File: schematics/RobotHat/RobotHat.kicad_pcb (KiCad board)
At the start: 2 copper layers, 65 x 63.5 mm, 43 parts, among them J1 9Vin, J10 MotorA, J11 MotorB, J12 Raspberry_Pi_2_3, J2 5Vout, J3 3V3out, J4 ATMega_ICSP, J5 ATMega_FTDI, J6 I2C, J7 ATMega AnalogPins, J8 WheelEncA, J9 WheelEncB, SW1 Reset, U1 ATmega328P-MU, U2 LM2596S-5, U3 TB6612FNG, Y1 16MHz

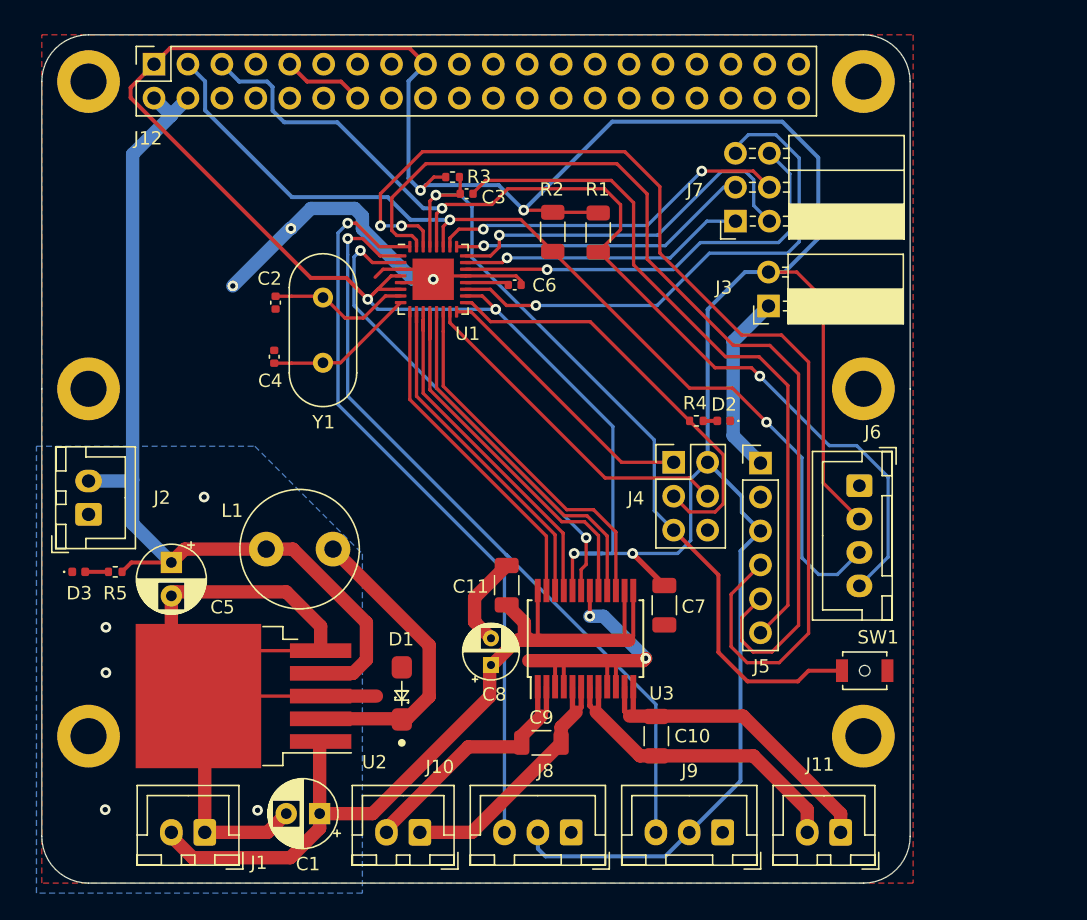
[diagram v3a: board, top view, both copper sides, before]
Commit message: Arduino runs at 5v with logic level shifter on i2c bus
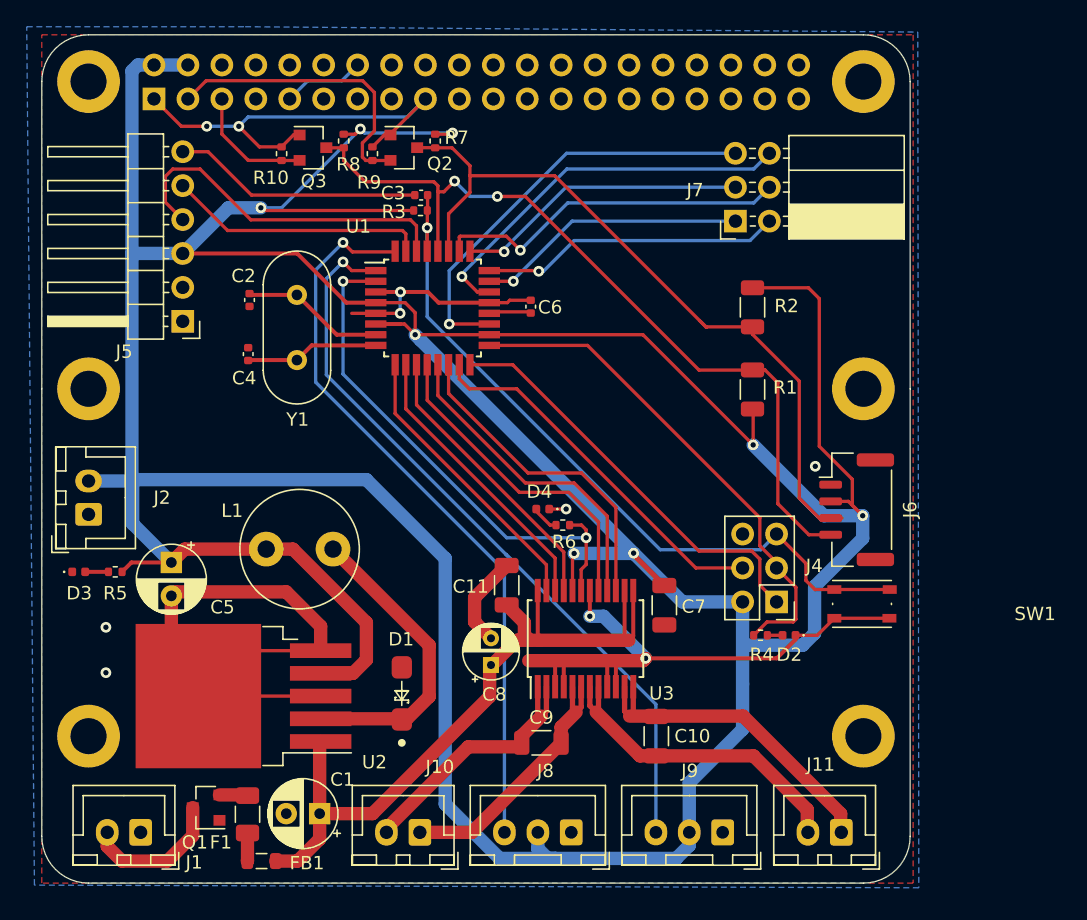
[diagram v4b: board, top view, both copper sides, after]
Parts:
- removed J3: 3V3out, Connector_PinSocket_2.54mm:PinSocket_1x02_P2.54mm_Horizontal
- added D4: GREEN, Diode_SMD:D_0402_1005Metric, F.Cu at (87.8, 77.5)
- added F1: Polyfuse, Fuse:Fuse_1206_3216Metric, F.Cu at (65.7, 100.3)
- added FB1: Ferrite_Bead, Inductor_SMD:L_0805_2012Metric, F.Cu at (66.8, 103.8)
- added Q1: AO3401A, Package_TO_SOT_SMD:SOT-23, F.Cu at (62.6, 99.8)
- added Q2: 2N7002, Package_TO_SOT_SMD:SOT-23, F.Cu at (77.4, 50.5)
- added Q3: 2N7002, Package_TO_SOT_SMD:SOT-23, F.Cu at (70.6, 50.5)
- added R10: 4.7k, Resistor_SMD:R_0402_1005Metric, F.Cu at (68.2, 50.9)
- added R6: 330, Resistor_SMD:R_0402_1005Metric, F.Cu at (89.3, 78.7)
- added R7: 4.7k, Resistor_SMD:R_0402_1005Metric, F.Cu at (79.8, 50.0)
- added R8: 4.7k, Resistor_SMD:R_0402_1005Metric, F.Cu at (72.9, 50.0)
- added R9: 4.7k, Resistor_SMD:R_0402_1005Metric, F.Cu at (75.0, 50.9)
- J12: moved to B.Cu
- J5: footprint Connector_PinHeader_2.54mm:PinHeader_1x06_P2.54mm_Vertical -> Connector_PinHeader_2.54mm:PinHeader_1x06_P2.54mm_Horizontal
- J6: footprint Connector_JST:JST_XH_B4B-XH-A_1x04_P2.50mm_Vertical -> Connector_JST:JST_GH_BM04B-GHS-TBT_1x04-1MP_P1.25mm_Vertical
- SW1: footprint Button_Switch_SMD:SW_SPST_B3U-1000P-B -> Button_Switch_SMD:SW_Push_1P1T_NO_Vertical_Wuerth_434133025816
- U1: value ATmega328P-MU -> ATmega328P-AU; footprint Package_DFN_QFN:QFN-32-1EP_5x5mm_P0.5mm_EP3.1x3.1mm -> Package_QFP:TQFP-32_7x7mm_P0.8mm
- moved J5 44.5 mm to (60.9, 63.5), turned to 180 degrees
- moved D2 16.8 mm to (106.2, 87.0)
- moved R4 16.8 mm to (104.1, 87.0)
- moved R1 16.5 mm to (103.5, 68.5), turned to 90 degrees
- moved R2 16.0 mm to (103.5, 62.4)
- moved J4 13.0 mm to (105.3, 84.5), turned to 180 degrees
- moved SW1 5.00 mm to (111.7, 84.6)
- moved J1 4.80 mm to (57.7, 101.7)
- moved R3 3.47 mm to (78.7, 55.1)
- moved C3 3.40 mm to (78.7, 54.0), turned to 0 degrees
- moved J12 2.60 mm to (58.7, 46.8), turned to 270 degrees
- moved U1 2.15 mm to (79.5, 62.5)
- moved C6 2.02 mm to (86.9, 62.4), turned to 270 degrees
- moved C2 1.96 mm to (65.8, 61.9)
- moved C4 1.96 mm to (65.8, 65.9)
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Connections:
- C1 pad 1: +9V -> +9VA
- C11 pad 1: +9V -> +9VA
- C7 pad 1: +3V3 -> +5V
- C8 pad 1: +9V -> +9VA
- J12 pad 3: SDA -> 3v3_SDA
- J12 pad 5: SCL -> 3v3_SCL
- J4 pad 2: +3V3 -> +5V
- J5 pad 3: +3V3 -> +5V
- J6 pad 2: +3V3 -> +5V
- J8 pad 2: +3V3 -> +5V
- J9 pad 2: +3V3 -> +5V
- R1 pad 1: +3V3 -> +5V
- R2 pad 1: +3V3 -> +5V
- R3 pad 1: +3V3 -> +5V
- U1 pad 18: +3V3 -> +5V
- U1 pad 4: +3V3 -> +5V
- U1 pad 6: +3V3 -> +5V
- U2 pad 1: +9V -> +9VA
- U3 pad 13: +9V -> +9VA
- U3 pad 14: +9V -> +9VA
- U3 pad 20: +3V3 -> +5V
- U3 pad 24: +9V -> +9VA
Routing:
- net +5V: track 70.7 -> 356.6 mm, vias 0 -> 8
- net +3V3: track 264.6 -> 33.1 mm, vias 6 -> 2
- net RXI: track 84.3 -> 26.5 mm, vias 2 -> 0
- net +9VA: track 0.00 -> 56.0 mm
- net TXO: track 73.9 -> 19.5 mm
- net +9V: track 64.2 -> 10.8 mm
- net DTR: track 52.5 -> 18.7 mm
- net GND: track 162.4 -> 133.2 mm, vias 10 -> 8
- net 3v3_SDA: track 0.00 -> 22.3 mm
- net SCL: track 81.4 -> 61.0 mm
- net SDA: track 74.7 -> 56.7 mm, vias 2 -> 0
- net MISO: track 20.9 -> 31.4 mm
- net 3v3_SCL: track 0.00 -> 9.27 mm
- net A6: track 40.3 -> 32.3 mm
- net RESET: track 61.8 -> 55.7 mm
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
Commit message: Hehe
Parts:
- removed C2, C4: 15pF, Capacitor_SMD:C_0402_1005Metric
- L1: footprint Inductor_THT:L_Radial_D8.7mm_P5.00mm_Fastron_07HCP -> RobotHat:YPRH1207-330M
- R10, R7, R8, R9: value 4.7k -> 10k
- Y1: value 16MHz -> 16Mhz; footprint Crystal:Crystal_HC49-4H_Vertical -> RobotHat:CSTCE16M0V53-R0
- moved L1 4.48 mm to (71.2, 78.7), turned to 90 degrees
- moved Y1 2.48 mm to (71.2, 64.7), turned to 270 degrees
- moved R10 0.90 mm to (67.3, 50.9)
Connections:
- Y1 pad 1: XTAL2 -> XTAL1
- Y1 pad 2: XTAL1 -> XTAL2
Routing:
- net GND: track 133.2 -> 142.3 mm
- net XTAL1: track 10.7 -> 4.41 mm
- net XTAL2: track 10.0 -> 4.24 mm
- net +5V: track 356.6 -> 358.1 mm

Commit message: other
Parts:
- removed F1: Polyfuse, Fuse:Fuse_1206_3216Metric
- removed FB1: Ferrite_Bead, Inductor_SMD:L_0805_2012Metric
- C1, C5: footprint Capacitor_THT:CP_Radial_D5.0mm_P2.50mm -> Capacitor_SMD:CP_Elec_6.3x7.7
- C10, C11, C7, C9: value 0.1uf -> 100nF
- C3, C6: value 0.1uF -> 100nF
- C8: footprint Capacitor_THT:CP_Radial_D4.0mm_P2.00mm -> Capacitor_SMD:CP_Elec_4x5.3
- J6: footprint Connector_JST:JST_GH_BM04B-GHS-TBT_1x04-1MP_P1.25mm_Vertical -> Connector_JST:JST_XH_B4B-XH-A_1x04_P2.50mm_Vertical
- R10, R3, R7, R8, R9: footprint Resistor_SMD:R_0402_1005Metric -> Resistor_SMD:R_0805_2012Metric
- moved SW1 4.85 mm to (111.8, 89.5)
- moved C5 2.32 mm to (62.2, 80.8)
- moved J6 2.32 mm to (112.0, 75.3)
- moved R7 2.13 mm to (81.8, 50.3)
- moved C8 1.66 mm to (82.5, 88.2)
- moved Q2 1.61 mm to (79.0, 50.2)
- moved J10 1.60 mm to (80.2, 101.8)
- moved C1 1.54 mm to (69.7, 101.0)
- moved Q3 1.51 mm to (69.1, 50.3)
- moved L1 1.36 mm to (72.5, 78.9)
- moved R9 1.32 mm to (76.2, 50.2)
- moved J8 1.32 mm to (91.2, 101.8)
- moved R10 1.25 mm to (66.2, 50.3)
- moved J9 1.03 mm to (102.3, 101.8)
- moved C3 1.00 mm to (78.7, 53.0)
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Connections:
- Q1 pad 2: Net-(F1-Pad2) -> +9VA
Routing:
- net GND: track 142.3 -> 121.2 mm, vias 8 -> 7
- net RESET: track 55.7 -> 61.0 mm
- net SCL: track 61.0 -> 66.1 mm
- net +9VA: track 56.0 -> 59.6 mm
- net +5V: track 358.1 -> 360.5 mm, vias 8 -> 7
- net Net-(F1-Pad2): track 2.12 -> 0.00 mm
- net Net-(F1-Pad1): track 2.11 -> 0.00 mm
- net +3V3: track 33.1 -> 31.0 mm, vias 2 -> 1
- net +9V: track 10.8 -> 8.89 mm
- net MOTORA1: track 20.3 -> 19.1 mm
- net SDA: track 56.7 -> 57.4 mm
- net Net-(D1-Pad1): track 22.7 -> 22.0 mm
- net D2: track 55.1 -> 55.7 mm
- net MOTORA2: track 20.2 -> 19.6 mm

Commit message: It
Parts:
- removed the R1 at (103.5, 68.5)
- removed the R2 at (103.5, 62.4)
- added C2: 22pF, Diode_SMD:D_0603_1608Metric, F.Cu at (65.6, 60.5)
- added C4: 22pF, Diode_SMD:D_0603_1608Metric, F.Cu at (65.6, 69.6)
- added J12: TFT_SPI_DISPLAY, Connector_PinHeader_2.54mm:PinHeader_2x05_P2.54mm_Vertical, F.Cu at (102.9, 63.0)
- C3, C6: footprint Capacitor_SMD:C_0402_1005Metric -> Capacitor_SMD:C_1206_3216Metric
- D2, D4: value GREEN -> RED; footprint Diode_SMD:D_0402_1005Metric -> Diode_SMD:D_0603_1608Metric
- D3: footprint Diode_SMD:D_0402_1005Metric -> Diode_SMD:D_0603_1608Metric
- R1: renamed from R3; footprint Resistor_SMD:R_0805_2012Metric -> Resistor_SMD:R_0603_1608Metric
- R2: renamed from R4; footprint Resistor_SMD:R_0402_1005Metric -> Resistor_SMD:R_0603_1608Metric
- R3: renamed from R5; footprint Resistor_SMD:R_0402_1005Metric -> Resistor_SMD:R_0603_1608Metric
- R4: renamed from R6; footprint Resistor_SMD:R_0402_1005Metric -> Resistor_SMD:R_0603_1608Metric
- R5: renamed from R9; footprint Resistor_SMD:R_0805_2012Metric -> Resistor_SMD:R_0603_1608Metric
- R6: renamed from R10; footprint Resistor_SMD:R_0805_2012Metric -> Resistor_SMD:R_0603_1608Metric
- R7, R8: footprint Resistor_SMD:R_0805_2012Metric -> Resistor_SMD:R_0603_1608Metric
- SW1: footprint Button_Switch_SMD:SW_Push_1P1T_NO_Vertical_Wuerth_434133025816 -> MyFootprints:TS-1187A-B-A-B_PushButton
- Y1: value 16Mhz -> Crystal; footprint RobotHat:CSTCE16M0V53-R0 -> Crystal:Crystal_HC49-4H_Vertical
- moved D4 16.7 mm to (98.7, 90.1), turned to 0 degrees
- moved R4 13.5 mm to (98.7, 88.4)
- moved C3 5.32 mm to (73.4, 53.5)
- moved Y1 2.93 mm to (69.3, 62.6)
- moved R2 1.83 mm to (102.3, 87.3)
- moved C6 1.57 mm to (88.4, 61.9), turned to 0 degrees
- moved D2 0.73 mm to (105.6, 87.3)
- moved SW1 0.71 mm to (111.2, 89.0), turned to 180 degrees
- moved D3 0.56 mm to (52.5, 82.2)
- moved R3 0.50 mm to (56.3, 82.2)
- moved R5 0.21 mm to (76.4, 50.2)
- moved R8 0.20 mm to (71.8, 50.3)
- moved R6 0.11 mm to (66.2, 50.4)
- moved R7 0.11 mm to (81.8, 50.4)
- renumbered J7 to J10, J12 to J11, J4 to J3, J5 to J4, J6 to J5, J8 to J6, J9 to J7, J10 to J8, J11 to J9
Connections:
- J11 pad 12: (no net) -> TFT_LED
- J11 pad 18: (no net) -> TFT_DCRS
- J11 pad 22: (no net) -> TFT_RESET
- J11 pad 24: (no net) -> TFT_CS
- J11 pad 35: (no net) -> RPI_MOSI
- J11 pad 38: (no net) -> RPI_MISO
- J11 pad 40: (no net) -> RPI_SCLK
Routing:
- net TFT_LED: track 0.00 -> 55.2 mm
- net TFT_CS: track 0.00 -> 42.5 mm
- net TFT_DCRS: track 0.00 -> 37.3 mm
- net GND: track 121.2 -> 156.9 mm, vias 7 -> 6
- net +3V3: track 31.0 -> 61.1 mm
- net TFT_RESET: track 0.00 -> 29.0 mm
- net +5V: track 360.5 -> 333.5 mm
- net RPI_MISO: track 0.00 -> 23.4 mm
- net RPI_SCLK: track 0.00 -> 21.3 mm
- net RPI_MOSI: track 0.00 -> 17.5 mm
- net D4: track 38.8 -> 52.9 mm, vias 2 -> 3
- net XTAL2: track 4.24 -> 11.2 mm
- net XTAL1: track 4.41 -> 11.0 mm
- net DTR: track 18.4 -> 12.2 mm
- net AREF: track 3.20 -> 7.93 mm
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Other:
- board text added: "3V"
- board text added: "5V"
- board text added: "9V"
- board text added: "A0"
- board text added: "A1"
- board text added: "A2"
- board text added: "A3"
- board text added: "A6"
- board text added: "A7"
- board text added: "B1"
- board text added: "B2"
- board text added: "CL"
- board text added: "CS"
- board text added: "DC"
- board text added: "DR"
- board text added: "EncodA"
- board text added: "EncodB"
- board text added: "G"
- board text added: "I2C"
- board text added: "ICSP"
- board text added: "LD"
- board text added: "MI"
- board text added: "MO"
- board text added: "MotorA"
- board text added: "MotorB"
- board text added: "R"
- board text added: "RX"
- board text added: "Reset"
- board text added: "S"
- board text added: "SC"
- board text added: "SD"
- board text added: "TFT_LCD_SPI"
- board text added: "TX"
